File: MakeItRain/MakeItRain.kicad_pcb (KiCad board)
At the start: 4 copper layers, 151.1 x 71.1 mm, 64 parts, among them IC1 OPA2340PA, IC2 LM2597MX-5.0_NOPB, J1 Conn_02x16_Odd_Even, J2 Conn_02x19_Odd_Even, J3 Conn_01x19, P1 Screw_Terminal_01x02, Q1 IRF9Z34NPBF, Q10 IRF9Z34NPBF, Q11 2N7000, Q12 2N7000, Q13 IRF9Z34NPBF, Q2 2N7000, Q3 2N7000, Q4 IRF9Z34NPBF, Q5 2N7000, Q6 2N7000, Q7 IRF9Z34NPBF, Q8 2N7000, Q9 2N7000, U1 178.6165.0001

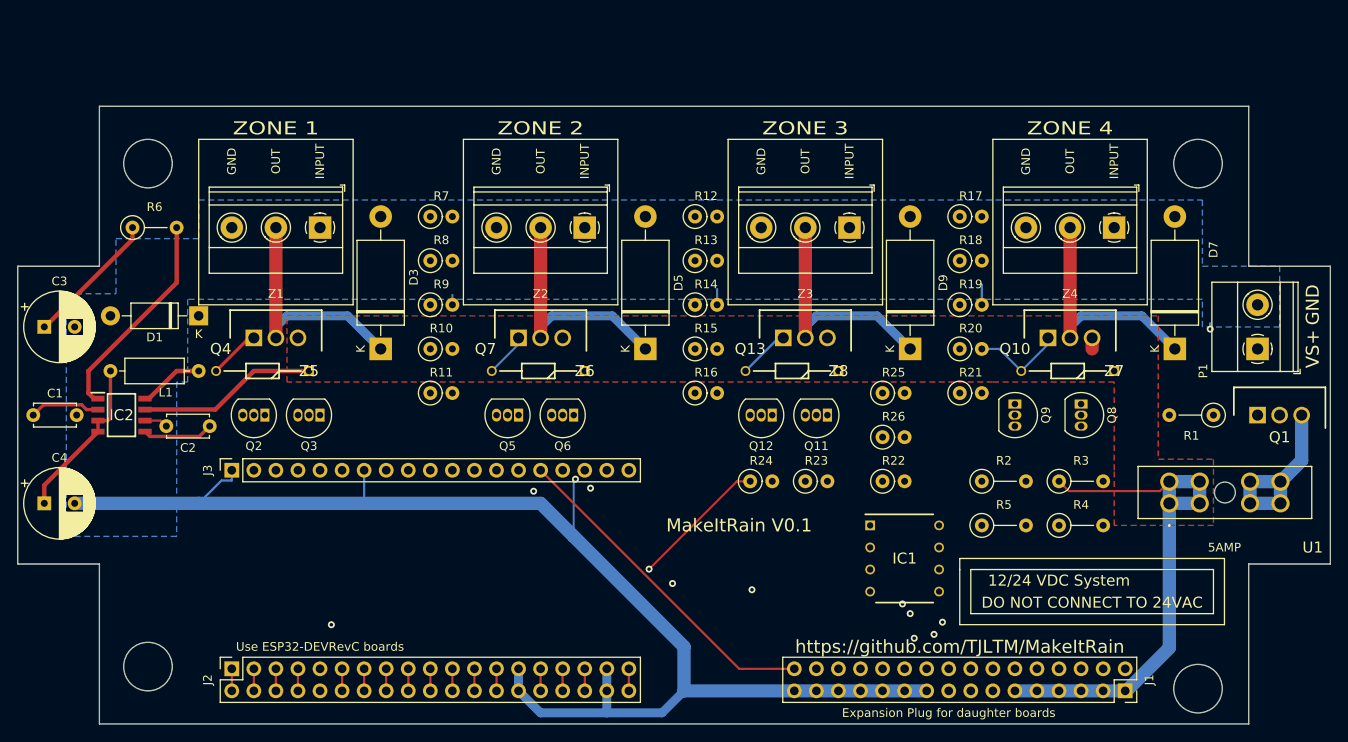
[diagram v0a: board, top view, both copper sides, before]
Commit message: WIP for HW fixed a few things like positions of the Power Fets so they can have a Heat sink. Added holes for mounting daughter boards. Feed Trace to Q1 was beefed up to wide zone from 10mils this is the main feed to the whole system.
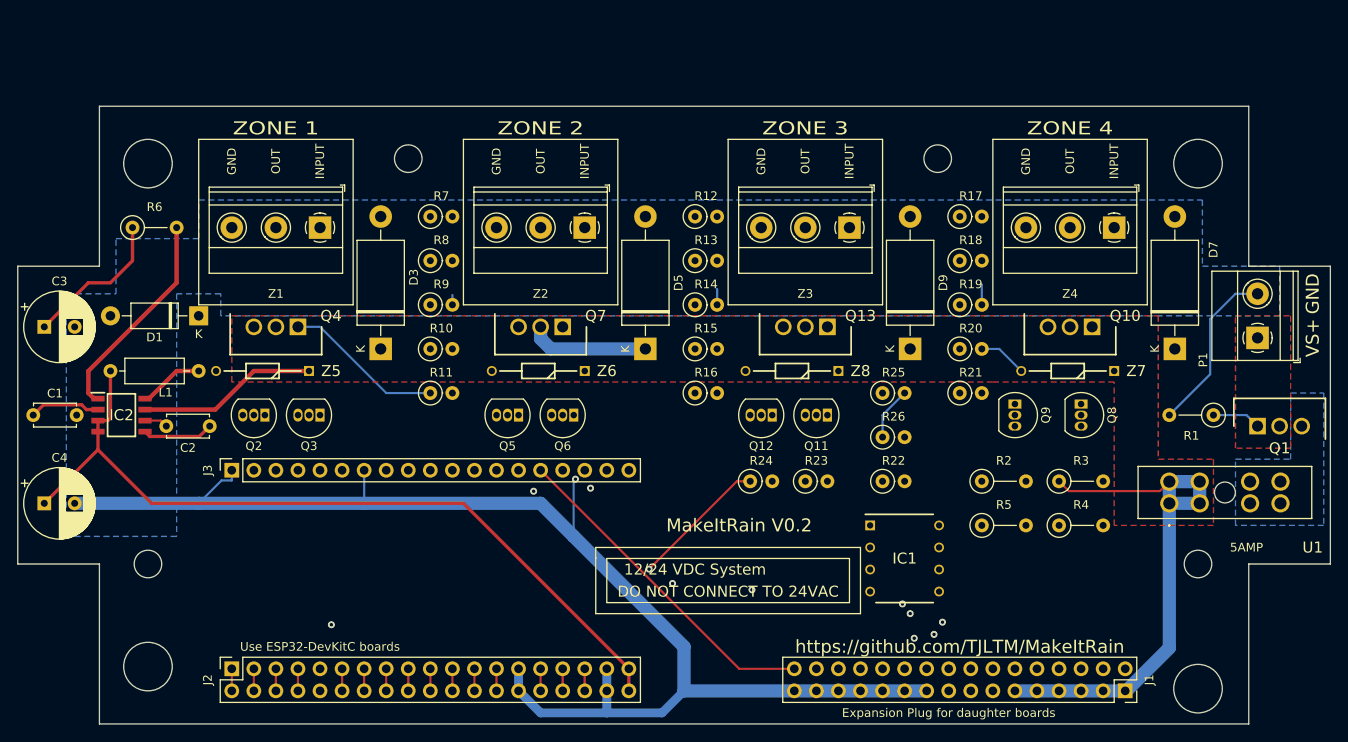
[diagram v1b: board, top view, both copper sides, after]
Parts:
- moved Q13 5.24 mm to (134.6, 81.3), turned to 180 degrees
- moved Q4 5.24 mm to (73.7, 81.3), turned to 180 degrees
- moved Q7 5.24 mm to (104.1, 81.3), turned to 180 degrees
- moved Q10 5.24 mm to (165.1, 81.3), turned to 180 degrees
- moved P1 1.27 mm to (184.2, 82.5)
- moved Q1 1.27 mm to (184.2, 92.7)
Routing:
- net Net-(Q1-Pad3): track 20.7 -> 0.00 mm
- net Net-(P1-Pad1): track 8.67 -> 0.00 mm
- net GND: track 281.2 -> 288.3 mm, vias 2 -> 1
- net +5V: track 100.1 -> 93.2 mm
- net Net-(Q10-Pad1): track 16.8 -> 22.0 mm
- net /Zone2IO/ZoneOutput: track 28.1 -> 25.3 mm
- net /Zone4IO/ZoneOutput: track 28.1 -> 30.4 mm
- net /Zone1IO/ZoneOutput: track 28.1 -> 30.4 mm
- net /Zone3IO/ZoneOutput: track 28.1 -> 30.4 mm
- net +VDC: track 163.8 -> 165.9 mm
- net Net-(Q13-Pad1): track 28.4 -> 29.7 mm
- net Net-(Q7-Pad1): track 36.6 -> 35.2 mm
- net Net-(Q4-Pad1): track 35.0 -> 36.1 mm
- net Net-(Q1-Pad1): track 5.08 -> 5.61 mm
- added copper zone on F.Cu, net Net-(P1-Pad1)
- added copper zone on B.Cu, net Net-(Q1-Pad3)
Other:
- outline, holes or cut-outs redrawn
- board text added: "MakeItRain V0.2"
- board text added: "Use ESP32-DevKitC boards"
- board text removed: "MakeItRain V0.1"
- board text removed: "Use ESP32-DEVRevC boards"

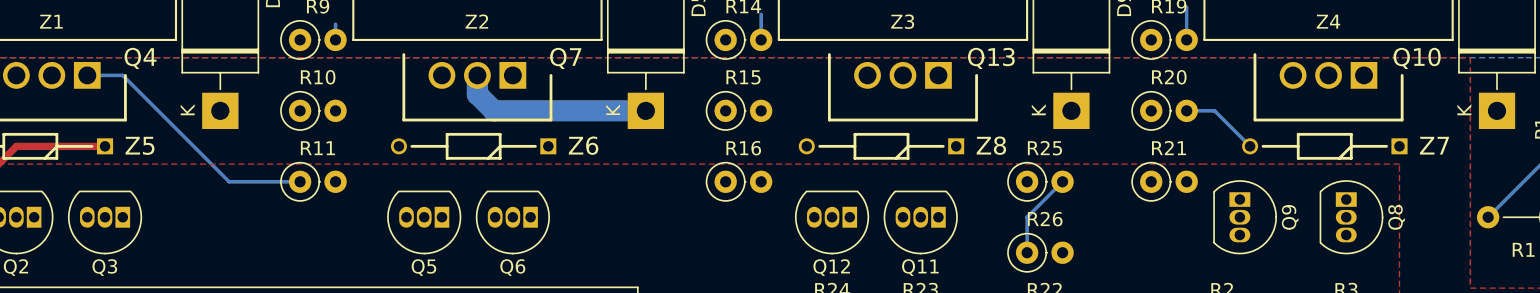
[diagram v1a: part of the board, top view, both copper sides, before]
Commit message: updated resistor values on the boards that weren't defined.
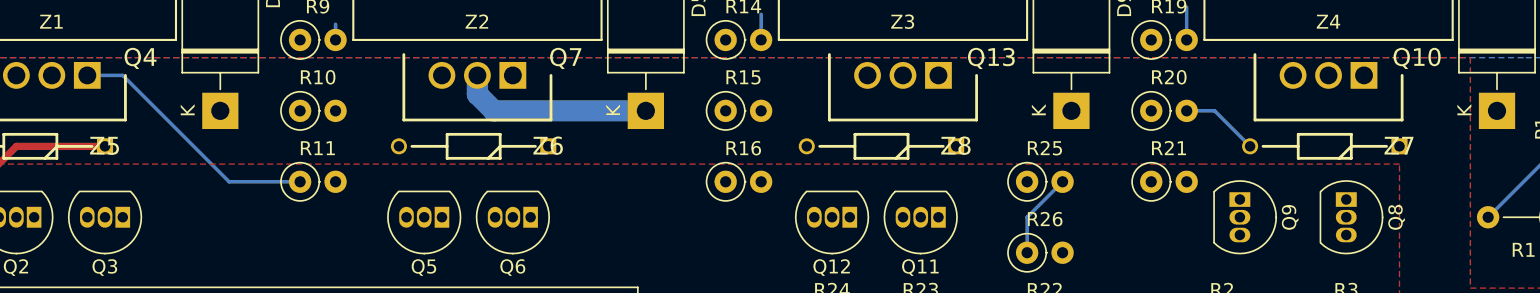
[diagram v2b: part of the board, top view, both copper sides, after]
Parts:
- R1: value R -> 10k

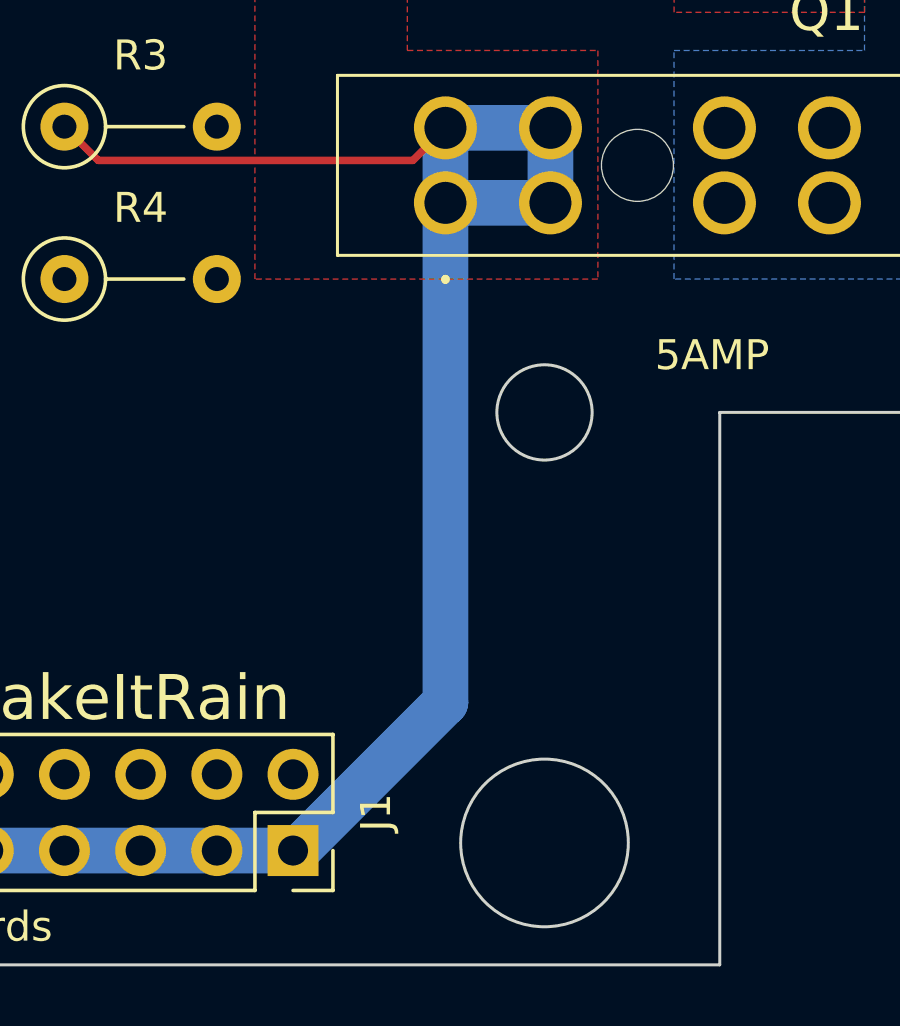
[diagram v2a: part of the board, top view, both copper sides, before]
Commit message: fixing a hole placement and routing.
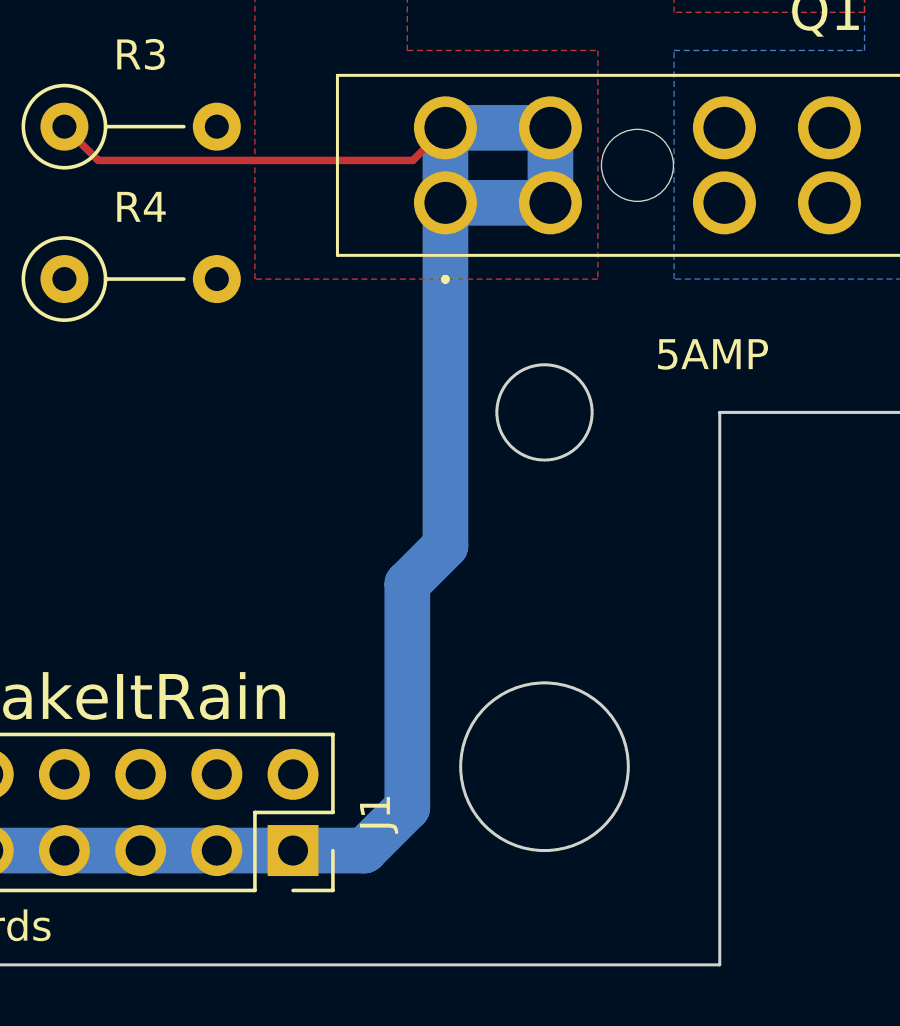
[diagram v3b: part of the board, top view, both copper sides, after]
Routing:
- net +VDC: track 165.9 -> 167.4 mm
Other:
- outline, holes or cut-outs redrawn

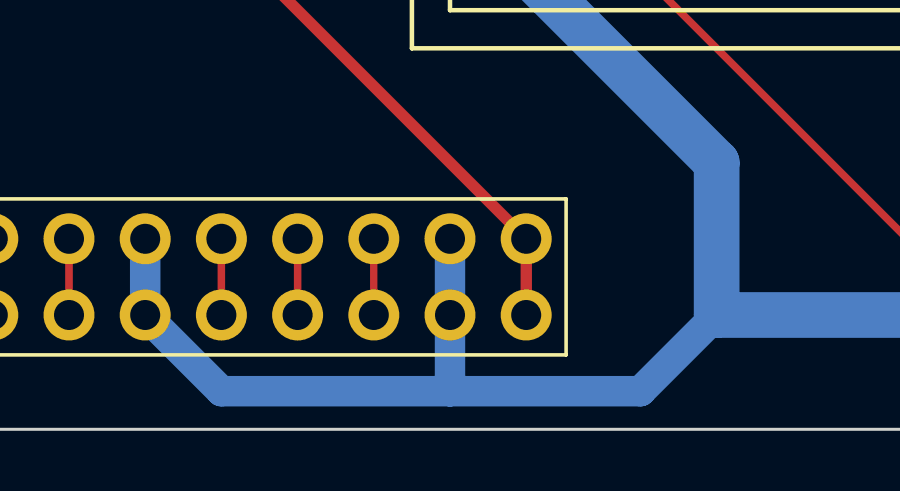
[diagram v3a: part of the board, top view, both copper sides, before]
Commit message: updated fab files and some values on the schematic. this is to fix the problem with grounding one of the ground pins and it affecting the dev board running and being able to load.
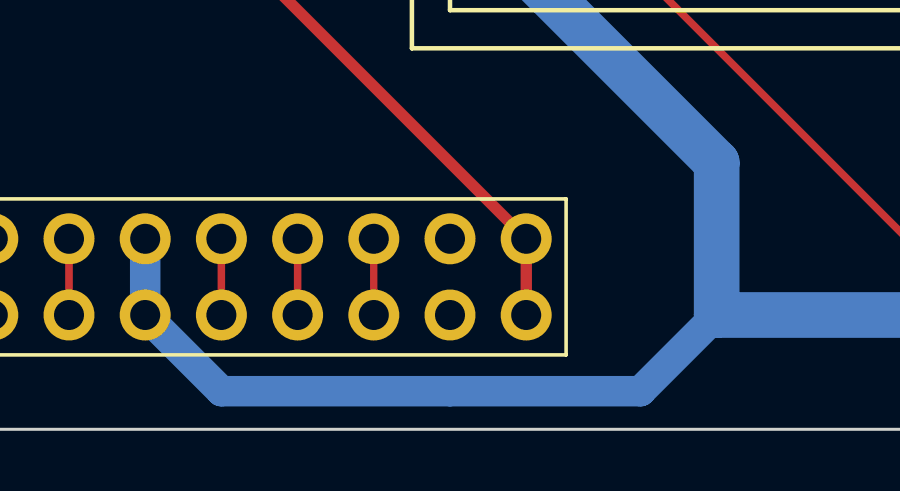
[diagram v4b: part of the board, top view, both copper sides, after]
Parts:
- C3: value CP1 -> 68uF
- C4: value CP1 -> 120uF
- R4: value 22k -> 15k
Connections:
- J2 pad 35: GND -> (no net)
- J2 pad 36: GND -> (no net)
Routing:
- net GND: track 288.3 -> 283.3 mm
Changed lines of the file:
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@@
     (thickness 1.6)
     (drawings 70)
-    (tracks 542)
+    (tracks 540)
     (zones 0)
     (modules 64)
@@
   )
   (setup
-    (last_trace_width 1.524)
+    (last_trace_width 0.25)
     (user_trace_width 0.381)
     (user_trace_width 0.508)
@@
       (drillshape 0)
       (scaleselection 1)
-      (outputdirectory "D:/REPOS/makeitrain/FabFiles"))
+      (outputdirectory "../FabFiles/"))
   )
   (net 0 "")
@@
       (effects (font (size 1 1) (thickness 0.15)))
     )
-    (fp_text value 22k (at 2.54 2.37) (layer F.Fab)
+    (fp_text value 15k (at 2.54 2.37) (layer F.Fab)
       (effects (font (size 1 1) (thickness 0.15)))
     )
@@
     (pad 37 thru_hole oval (at 0 45.72 90) (size 1.7 1.7) (drill 1) (layers *.Cu *.Mask)
       (net 5 +5V))
-    (pad 36 thru_hole oval (at -2.54 43.18 90) (size 1.7 1.7) (drill 1) (layers *.Cu *.Mask)
-      (net 1 GND))
-    (pad 35 thru_hole oval (at 0 43.18 90) (size 1.7 1.7) (drill 1) (layers *.Cu *.Mask)
-      (net 1 GND))
+    (pad 36 thru_hole oval (at -2.54 43.18 90) (size 1.7 1.7) (drill 1) (layers *.Cu *.Mask))
+    (pad 35 thru_hole oval (at 0 43.18 90) (size 1.7 1.7) (drill 1) (layers *.Cu *.Mask))
     (pad 34 thru_hole oval (at -2.54 40.64 90) (size 1.7 1.7) (drill 1) (layers *.Cu *.Mask)
       (net 11 /SD3))
@@
       (effects (font (size 1 1) (thickness 0.15)))
     )
-    (fp_text value CP1 (at 1.75 5.25) (layer F.Fab)
+    (fp_text value 120uF (at 1.75 5.25) (layer F.Fab)
       (effects (font (size 1 1) (thickness 0.15)))
     )
@@
       (effects (font (size 1 1) (thickness 0.15)))
     )
-    (fp_text value CP1 (at 1.75 5.25) (layer F.Fab)
+    (fp_text value 68uF (at 1.75 5.25) (layer F.Fab)
       (effects (font (size 1 1) (thickness 0.15)))
     )
@@
   (segment (start 138.43 123.19) (end 140.97 123.19) (width 1.524) (layer B.Cu) (net 1))
   (segment (start 140.97 123.19) (end 143.51 123.19) (width 1.524) (layer B.Cu) (net 1))
-  (segment (start 109.22 123.19) (end 109.22 120.65) (width 1.016) (layer B.Cu) (net 1))
-  (segment (start 109.22 125.73) (end 109.22 123.19) (width 1.016) (layer B.Cu) (net 1))
   (segment (start 118.11 123.19) (end 115.57 125.73) (width 1.016) (layer B.Cu) (net 1))
   (segment (start 115.57 125.73) (end 109.22 125.73) (width 1.016) (layer B.Cu) (net 1))

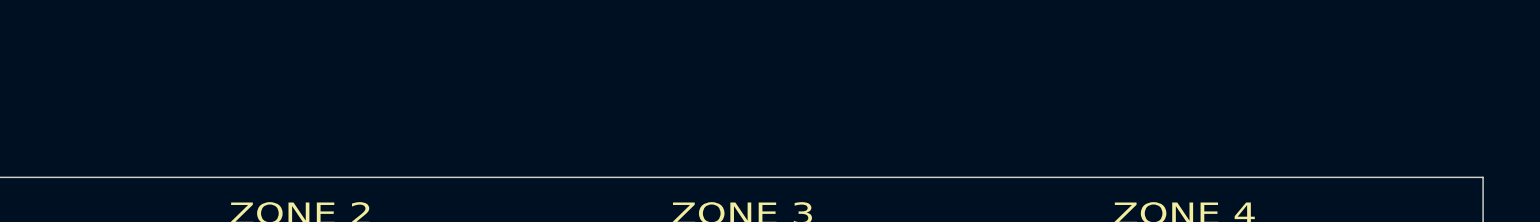
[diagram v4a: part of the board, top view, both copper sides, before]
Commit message: adding the debounce caps haven't moved some stuff around on the board to fit these in.
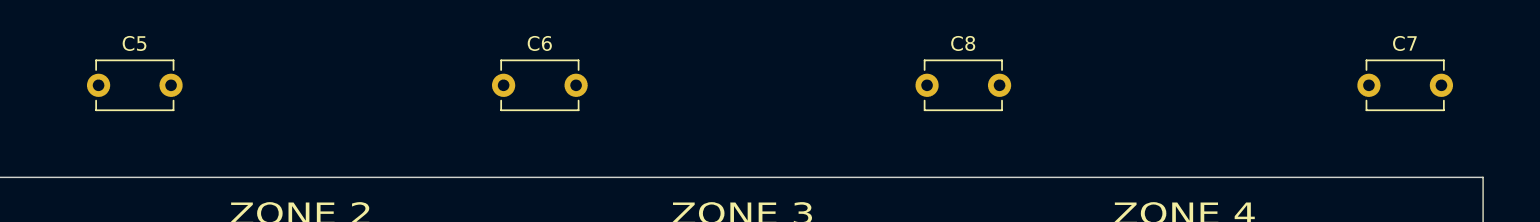
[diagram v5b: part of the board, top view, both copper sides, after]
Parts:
- added C5: 220nF, Capacitor_THT:C_Disc_D5.1mm_W3.2mm_P5.00mm, F.Cu at (87.6, 49.5)
- added C6: 220nF, Capacitor_THT:C_Disc_D5.1mm_W3.2mm_P5.00mm, F.Cu at (115.6, 49.5)
- added C7: 220nF, Capacitor_THT:C_Disc_D5.1mm_W3.2mm_P5.00mm, F.Cu at (175.3, 49.5)
- added C8: 220nF, Capacitor_THT:C_Disc_D5.1mm_W3.2mm_P5.00mm, F.Cu at (144.8, 49.5)

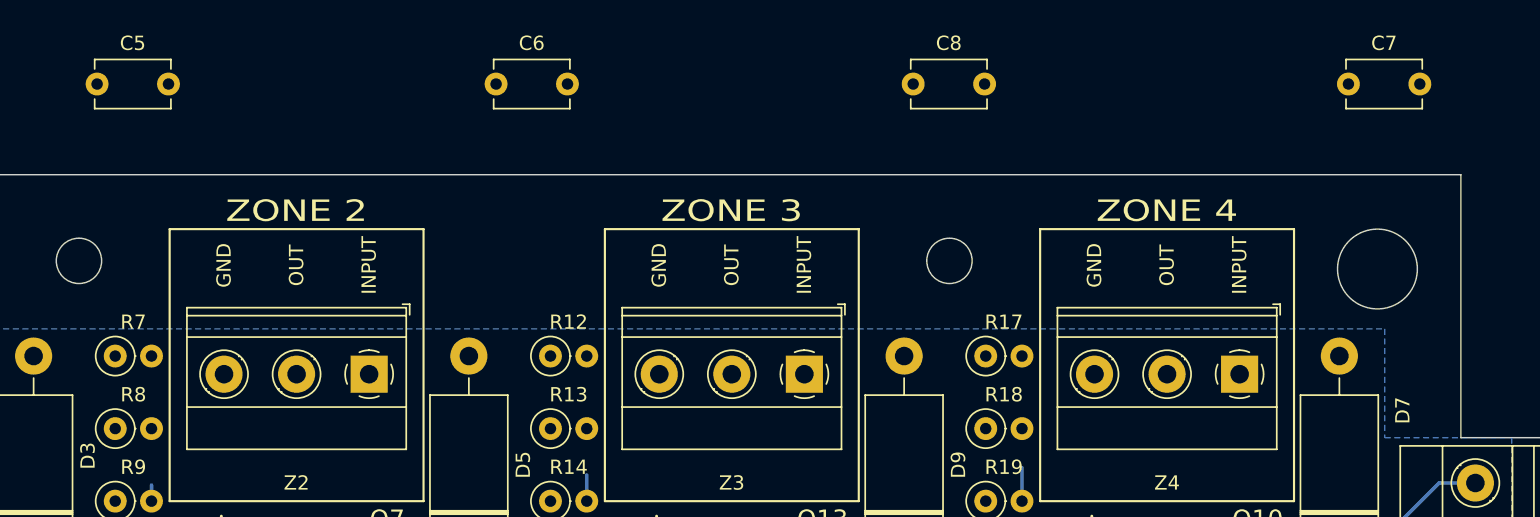
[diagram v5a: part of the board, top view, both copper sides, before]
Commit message: added the debounce caps to the layout and updated the fab files for this version.
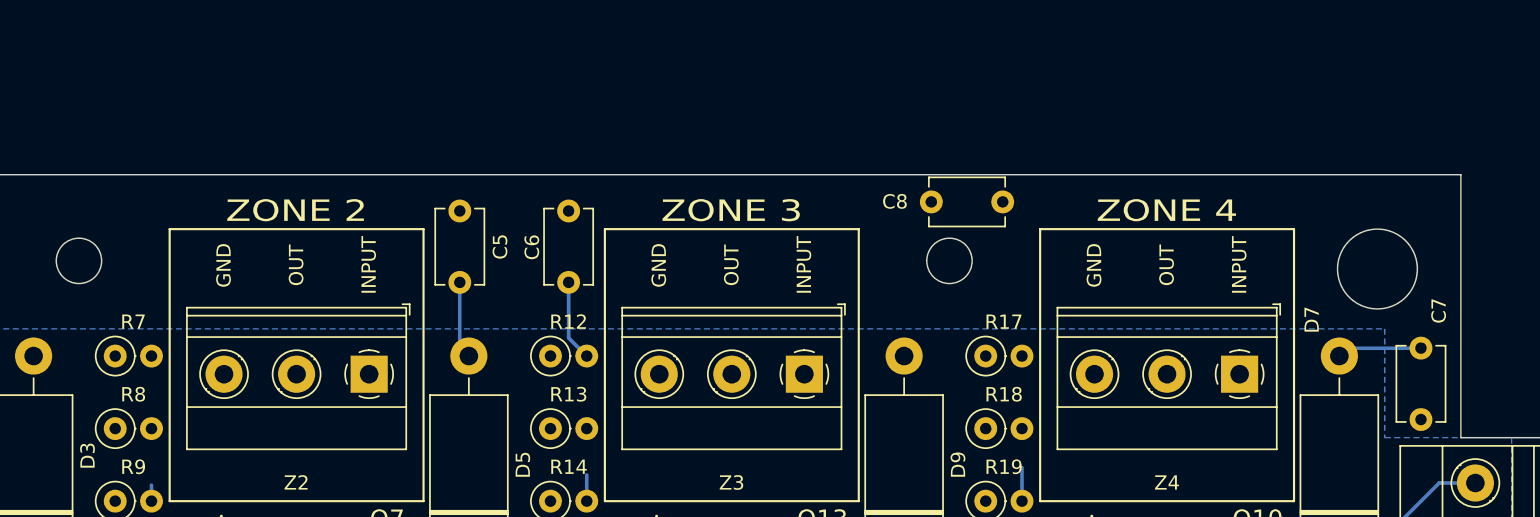
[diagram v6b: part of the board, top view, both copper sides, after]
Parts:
- moved C5 26.9 mm to (113.0, 58.4), turned to 270 degrees
- moved C7 24.0 mm to (180.3, 73.0), turned to 90 degrees
- moved C6 10.2 mm to (120.7, 58.4), turned to 270 degrees
- moved C8 8.35 mm to (146.1, 57.8)
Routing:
- net GND: track 283.3 -> 311.7 mm
- net /Zone1IO/ZoneInput: track 38.3 -> 66.6 mm
- net /Zone3IO/ZoneInput: track 38.8 -> 55.3 mm
- net /Zone4IO/ZoneInput: track 43.8 -> 55.9 mm
- net /Zone2IO/ZoneInput: track 38.8 -> 50.6 mm

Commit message: update to kicad 6.0 and start on adding in opto-isolationg to the inputs as to protect the processor GPIO
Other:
- net class Default removed
